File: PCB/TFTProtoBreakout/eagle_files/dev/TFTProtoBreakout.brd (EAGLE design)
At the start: 32.9 x 63.5 mm, 13 parts, among them SW1 PCM12SMTR, SW2 PCM12SMTR, SW3 PCM12SMTR, SW4 PCM12SMTR

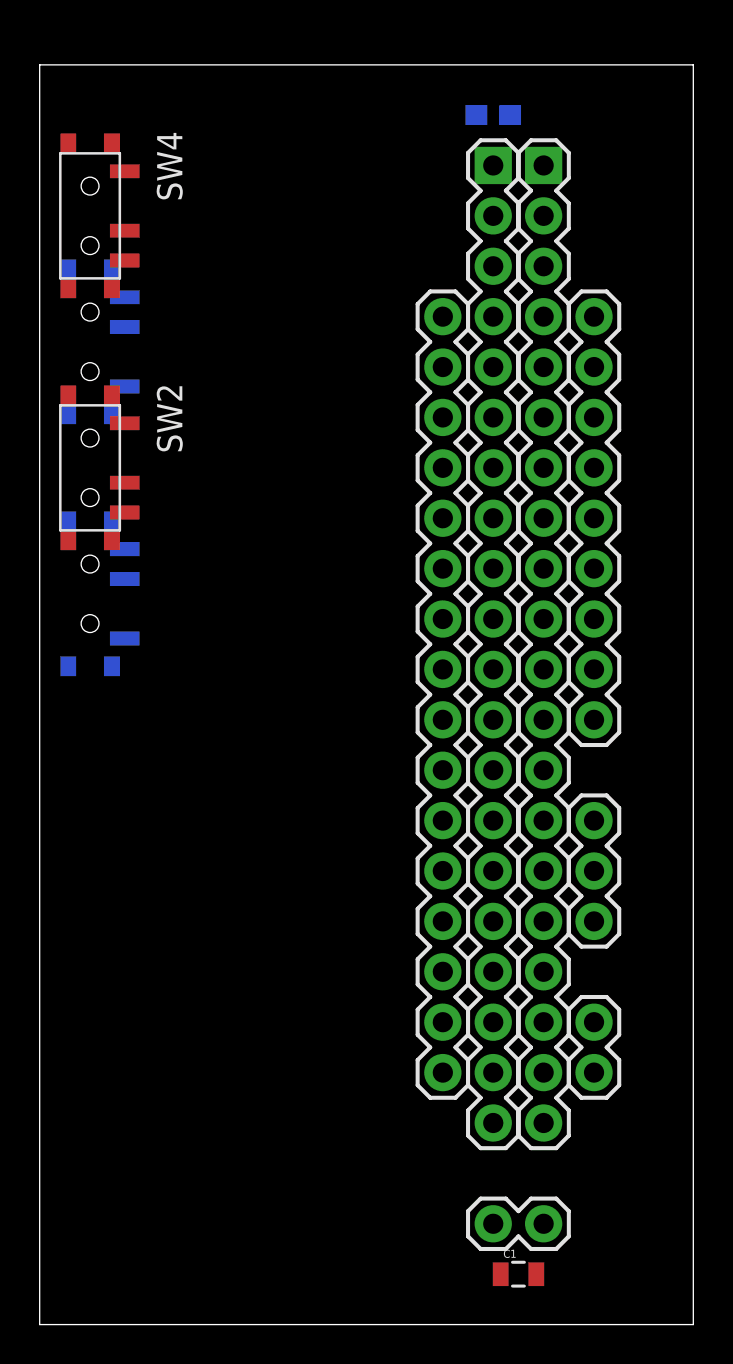
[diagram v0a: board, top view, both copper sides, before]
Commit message: Added first cut of trace routing to board design. A bit messy, but functional.
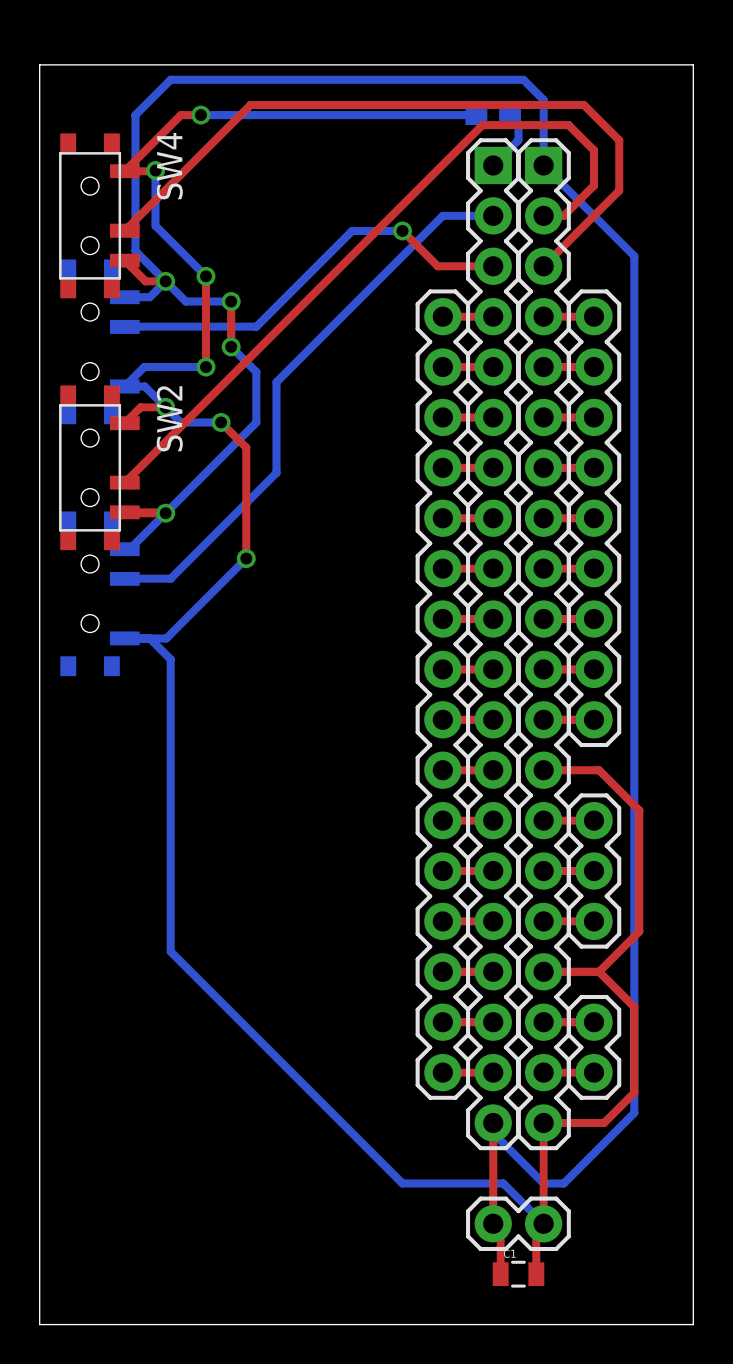
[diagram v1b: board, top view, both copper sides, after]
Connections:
- removed net LEDA: C1.1, JP1.20, JP2.1, JP7.2
- net VCC: now also C1.1, JP1.20, JP2.1, JP7.2
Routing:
- net GND: track 0.00 -> 138.3 mm, vias 0 -> 7
- net VCC: track 0.00 -> 130.3 mm, vias 0 -> 4
- net IM1: track 0.00 -> 36.6 mm
- net IM3: track 0.00 -> 36.2 mm
- net IM0: track 0.00 -> 28.8 mm
- net IM2: track 0.00 -> 21.3 mm, vias 0 -> 1
- net LEDK: track 0.00 -> 3.24 mm
- net Y-: track 0.00 -> 2.54 mm
- net Y+: track 0.00 -> 2.54 mm
- net SDI: track 0.00 -> 2.54 mm
- net NWR_SCL: track 0.00 -> 2.54 mm
- net NCS: track 0.00 -> 2.54 mm
- net D9: track 0.00 -> 2.54 mm
- net D7: track 0.00 -> 2.54 mm
- net D5: track 0.00 -> 2.54 mm
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
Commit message: Modified to be a bit more clean.
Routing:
- net GND: track 138.3 -> 146.5 mm, vias 7 -> 5
- net IM1: track 36.6 -> 41.5 mm
- net IM0: track 28.8 -> 32.7 mm
- net IM2: track 21.3 -> 19.8 mm
- net VCC: track 130.3 -> 130.8 mm, vias 4 -> 6

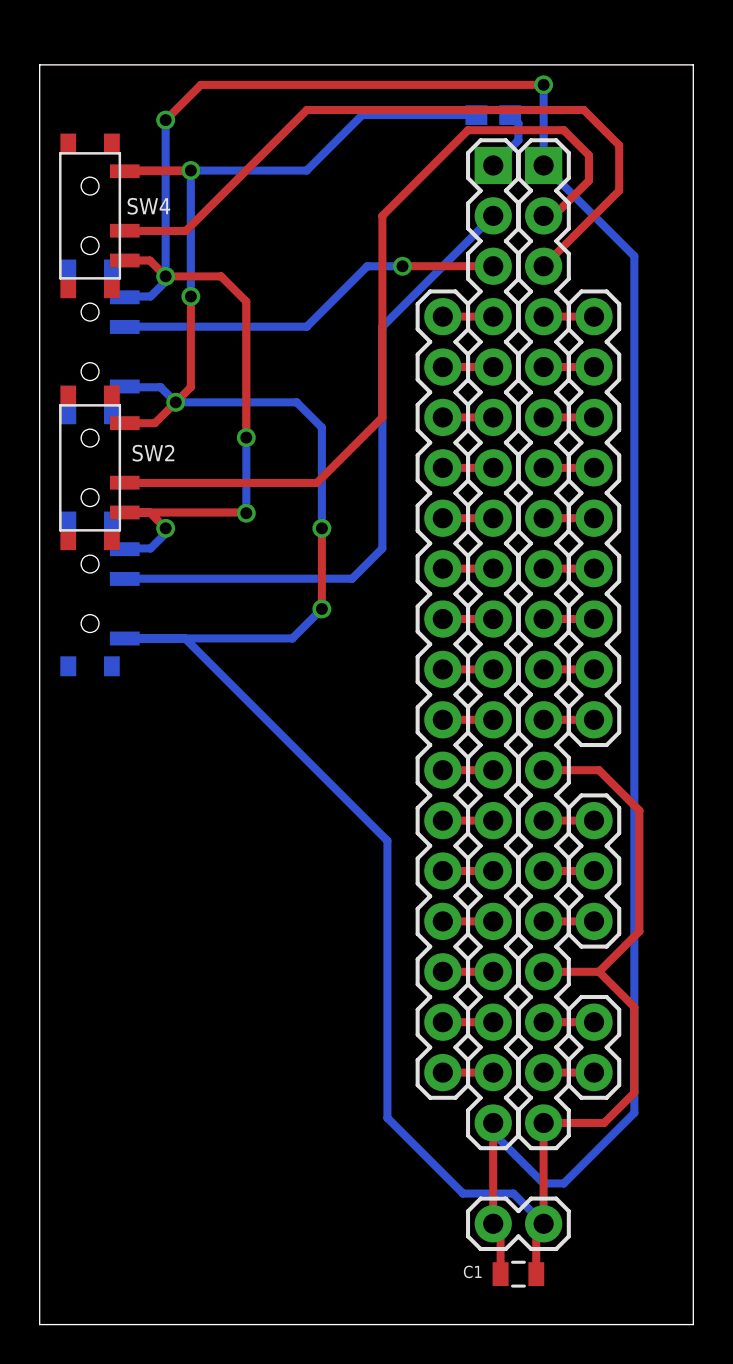
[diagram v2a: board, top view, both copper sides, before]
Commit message: Added pin labels and rerouted to work around these a bit more cleanly. Also included note about switch todo.
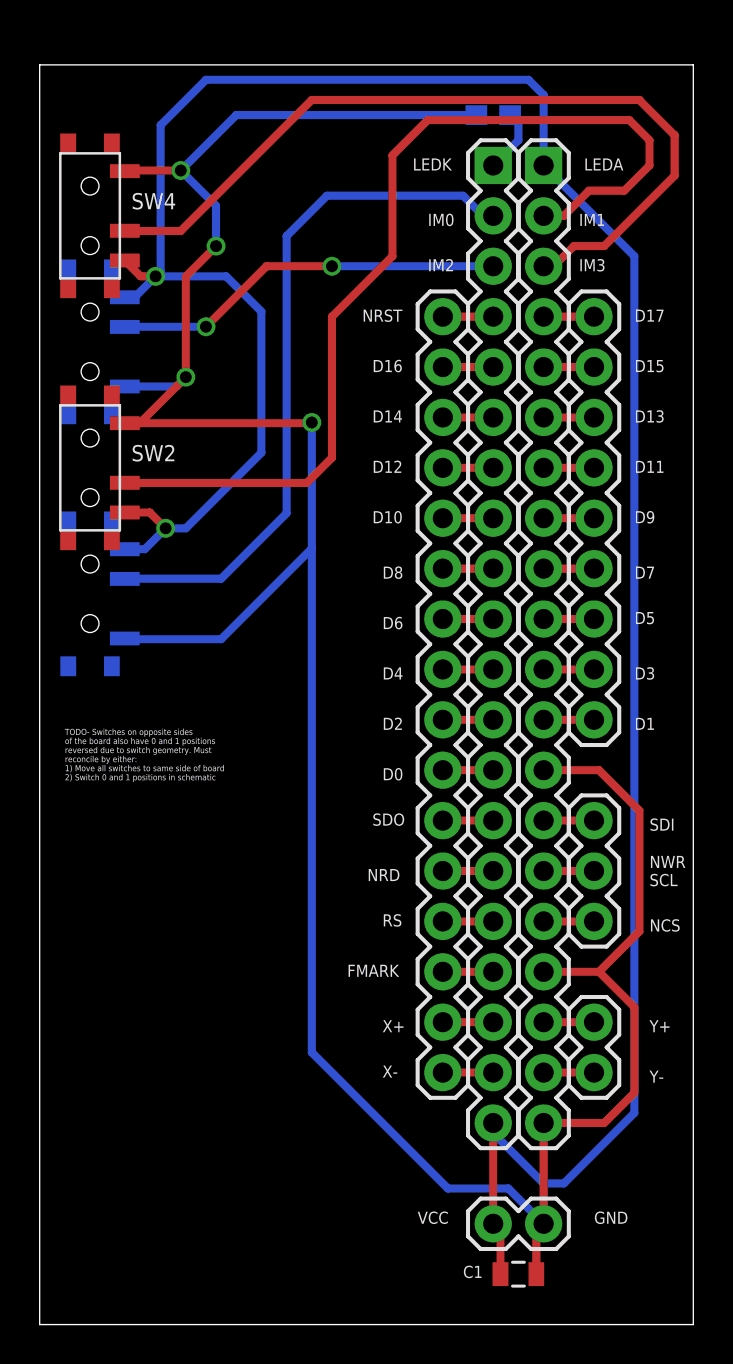
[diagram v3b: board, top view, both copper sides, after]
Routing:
- net IM1: track 41.5 -> 49.2 mm
- net IM3: track 35.9 -> 41.7 mm
- net GND: track 146.5 -> 143.0 mm, vias 5 -> 4
- net VCC: track 130.8 -> 127.8 mm, vias 6 -> 2
- net IM0: track 32.7 -> 35.2 mm
- net IM2: vias 1 -> 2
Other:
- board text added: "D0"
- board text added: "D1"
- board text added: "D10"
- board text added: "D11"
- board text added: "D12"
- board text added: "D13"
- board text added: "D14"
- board text added: "D15"
- board text added: "D16"
- board text added: "D17"
- board text added: "D2"
- board text added: "D3"
- board text added: "D4"
- board text added: "D5"
- board text added: "D6"
- board text added: "D7"
- board text added: "D8"
- board text added: "D9"
- board text added: "FMARK"
- board text added: "GND"
- board text added: "IM0"
- board text added: "IM1"
- board text added: "IM2"
- board text added: "IM3"
- board text added: "LEDA"
- board text added: "LEDK"
- board text added: "NCS"
- board text added: "NRD"
- board text added: "NRST"
- board text added: "NWR SCL"
- board text added: "RS"
- board text added: "SDI"
- board text added: "SDO"
- board text added: "TODO- Switches on opposite sides of the board also have 0 and 1 positions reversed due to switch geometry. Must reconcile by either: 1) Move all switches to same side of board 2) Switch 0 and 1 positions in schematic"
- board text added: "VCC"
- board text added: "X+"
- board text added: "X-"
- board text added: "Y+"
- board text added: "Y-"

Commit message: Laid switches on one face abreast and routed.
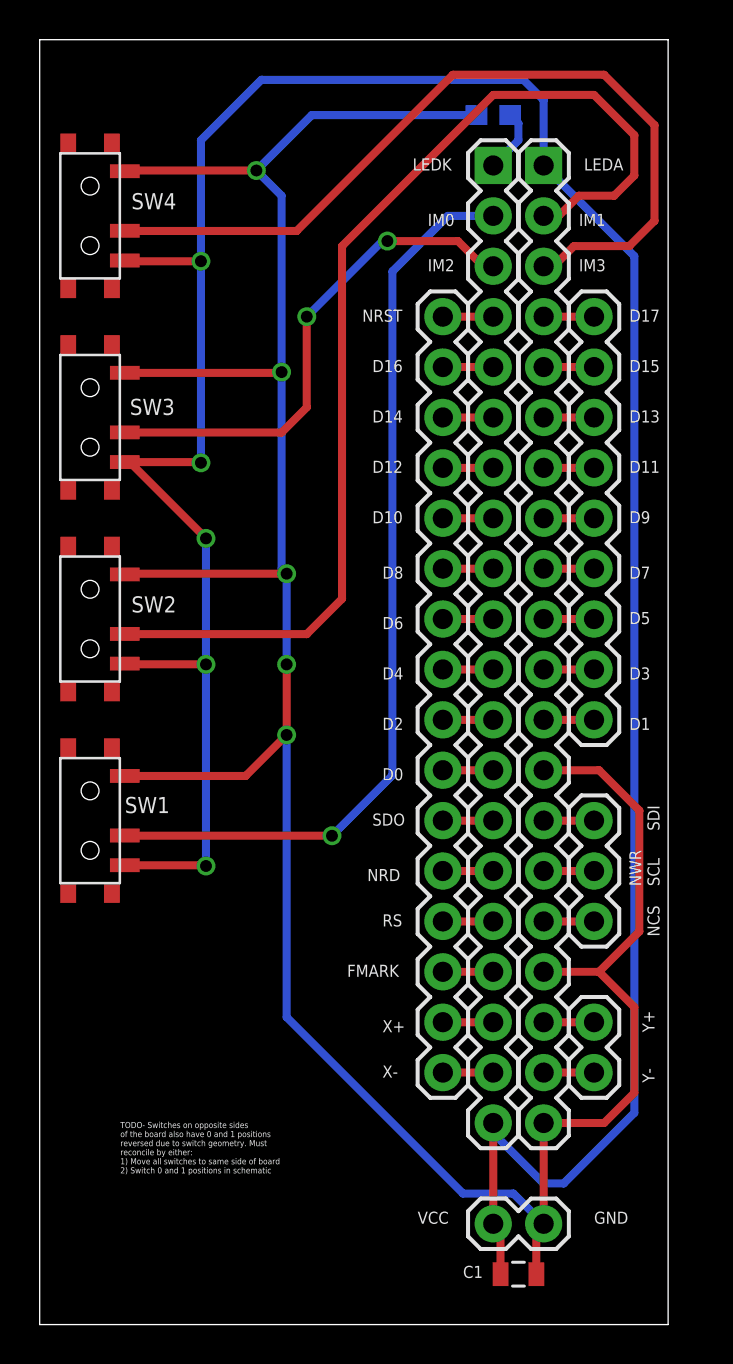
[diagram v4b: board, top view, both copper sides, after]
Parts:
- moved SW1 11.4 mm to (2.54, 25.4), flipped to the top, turned to 270 degrees
- moved SW2 7.62 mm to (2.54, 35.6)
- moved SW3 3.81 mm to (2.54, 45.7), flipped to the top, turned to 270 degrees
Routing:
- net VCC: track 127.8 -> 144.2 mm, vias 2 -> 5
- net IM0: track 35.2 -> 46.4 mm, vias 0 -> 1
- net IM1: track 49.2 -> 55.6 mm
- net IM2: track 19.8 -> 25.8 mm
- net GND: track 143.0 -> 141.8 mm, vias 4 -> 5
- net IM3: track 41.7 -> 42.4 mm
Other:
- board size 32.9 x 63.5 mm -> 31.7 x 64.8 mm

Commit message: Finalize routing to be more clean. Add keyhole for Power connections and Add labels.
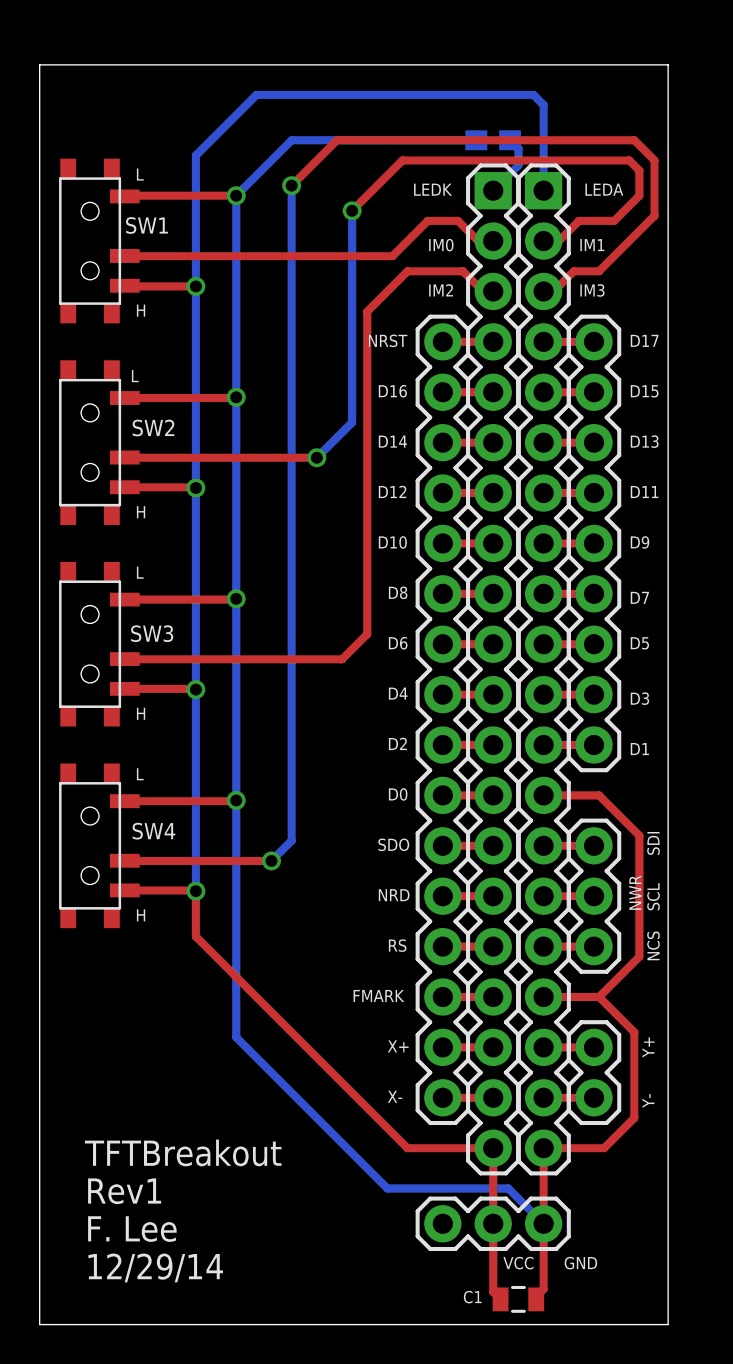
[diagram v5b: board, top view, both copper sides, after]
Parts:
- JP7: value M02PTH -> (none); device SparkFun-Connectors:1X02 -> SparkFun-Connectors:1X03
- moved SW4 31.8 mm to (2.54, 24.1)
- moved SW1 29.2 mm to (2.54, 54.6)
- moved SW3 11.4 mm to (2.54, 34.3)
- moved SW2 8.89 mm to (2.54, 44.5)
- moved JP1 1.27 mm to (22.9, 57.1)
- moved JP2 1.27 mm to (25.4, 57.1)
- moved R1 1.27 mm to (22.9, 59.7)
- moved C1 1.27 mm to (24.1, 1.27)
- moved JP3 1.27 mm to (20.3, 11.4)
- moved JP4 1.27 mm to (27.9, 11.4)
- moved JP5 1.27 mm to (27.9, 19.1)
- moved JP6 1.27 mm to (27.9, 29.2)
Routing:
- net VCC: track 144.2 -> 104.3 mm, vias 5 -> 4
- net IM3: track 42.4 -> 71.5 mm, vias 0 -> 2
- net IM0: track 46.4 -> 19.7 mm, vias 1 -> 0
- net IM2: track 25.8 -> 36.6 mm, vias 2 -> 0
- net IM1: track 55.6 -> 45.7 mm, vias 0 -> 2
- net GND: track 141.8 -> 134.8 mm, vias 5 -> 4
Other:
- board size 31.7 x 64.8 mm -> 31.7 x 63.5 mm
- board text added: "H"
- board text added: "L"
- board text added: "TFTBreakout Rev1 F. Lee 12/29/14"
- board text removed: "TODO- Switches on opposite sides of the board also have 0 and 1 positions reversed due to switch geometry. Must reconcile by either: 1) Move all switches to same side of board 2) Switch 0 and 1 positions in schematic"
